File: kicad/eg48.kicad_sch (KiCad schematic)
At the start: 110 parts, among them SW1 PG1350, SW10 PG1350, SW11 PG1350, SW12 PG1350, SW13 PG1350, SW14 PG1350, SW15 PG1350, SW16 PG1350, SW17 PG1350, SW18 PG1350, SW19 PG1350, SW2 PG1350, SW20 PG1350, SW21 PG1350, SW22 PG1350, SW23 PG1350, SW24 PG1350, SW25 PG1350, SW26 PG1350, SW27 PG1350, SW28 PG1350, SW29 PG1350, SW3 PG1350, SW30 PG1350, SW31 PG1350, SW32 PG1350, SW33 PG1350, SW34 PG1350, SW35 PG1350, SW36 PG1350, SW37 PG1350, SW38 PG1350, SW39 PG1350, SW4 PG1350, SW40 PG1350, SW41 PG1350, SW42 PG1350, SW43 PG1350, SW44 PG1350, SW45 PG1350, SW46 PG1350, SW47 PG1350, SW48 PG1350, SW49 RotaryEncoder_Switch_MP, SW5 PG1350, SW6 PG1350, SW7 PG1350, SW8 PG1350, SW9 PG1350

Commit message: Update kicad files, add 3D models
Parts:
- SW49: value RotaryEncoder_Switch_MP -> EC11E12
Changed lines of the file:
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@@
 			)
 		)
-		(property "Value" "RotaryEncoder_Switch_MP"
+		(property "Value" "EC11E12"
 			(at 52.07 77.4699 90)
 			(effects

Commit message: Kicad 9, nicer routing, clearance for rp2040
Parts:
- U1: value ~ -> Pro Micro RP2040; footprint pro_micro_rp2040:pro_micro_rp2040 -> pro_micro_rp2040:pro_micro_rp2040_min; symbol pro_micro_rp2040:pro_micro_rp2040 -> pro_micro_rp2040:pro_micro_rp2040_min
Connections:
- no-connect marks 13 -> 9
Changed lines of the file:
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@@
 (kicad_sch
-	(version 20231120)
+	(version 20250114)
 	(generator "eeschema")
-	(generator_version "8.0")
+	(generator_version "9.0")
 	(paper "A4")
 	(junction
@@
 	)
 	(no_connect
-		(at 50.8 21.59)
-	)
-	(no_connect
 		(at 29.21 54.61)
 	)
 	(no_connect
-		(at 45.72 21.59)
-	)
-	(no_connect
 		(at 40.64 62.23)
 	)
 	(no_connect
-		(at 43.18 21.59)
-	)
-	(no_connect
-		(at 48.26 21.59)
-	)
-	(no_connect
 		(at 60.96 26.67)
 	)
@@
 	(label "ROW9"
 		(at 53.34 64.77 0)
-		(fields_autoplaced yes)
 		(effects
 			(font
@@
 	(label "COL2"
 		(at 63.5 41.91 0)
-		(fields_autoplaced yes)
 		(effects
 			(font
@@
 	(label "COL1"
 		(at 63.5 44.45 0)
-		(fields_autoplaced yes)
 		(effects
 			(font
@@
 	(label "COL5"
 		(at 29.21 29.21 180)
-		(fields_autoplaced yes)
 		(effects
 			(font
@@
 	(label "COL4"
 		(at 80.01 104.14 90)
-		(fields_autoplaced yes)
 		(effects
 			(font
@@
 	(label "COL3"
 		(at 63.5 39.37 0)
-		(fields_autoplaced yes)
 		(effects
 			(font
@@
 	(label "ROW2"
 		(at 142.24 114.3 180)
-		(fields_autoplaced yes)
 		(effects
 			(font
@@
 	(label "COL3"
 		(at 64.77 104.14 90)
-		(fields_autoplaced yes)
 		(effects
 			(font
@@
 	(label "COL6"
 		(at 220.98 104.14 90)
-		(fields_autoplaced yes)
 		(effects
 			(font
@@
 	(label "COL6"
 		(at 110.49 104.14 90)
-		(fields_autoplaced yes)
 		(effects
 			(font
@@
 	(label "ROW7"
 		(at 123.19 160.02 0)
-		(fields_autoplaced yes)
 		(effects
 			(font
@@
 	(label "ROW6"
 		(at 142.24 144.78 180)
-		(fields_autoplaced yes)
 		(effects
 			(font
@@
 	(label "ROW4"
 		(at 63.5 49.53 0)
-		(fields_autoplaced yes)
 		(effects
 			(font
@@
 	(label "COL1"
 		(at 144.78 104.14 90)
-		(fields_autoplaced yes)
 		(effects
 			(font
@@
 	(label "COL5"
 		(at 95.25 104.14 90)
-		(fields_autoplaced yes)
 		(effects
 			(font
@@
 	(label "ROW2"
 		(at 63.5 46.99 0)
-		(fields_autoplaced yes)
 		(effects
 			(font
@@
 	(label "COL4"
 		(at 29.21 26.67 180)
-		(fields_autoplaced yes)
 		(effects
 			(font
@@
 	(label "COL2"
 		(at 160.02 104.14 90)
-		(fields_autoplaced yes)
 		(effects
 			(font
@@
 	(label "ROW8"
 		(at 142.24 160.02 180)
-		(fields_autoplaced yes)
 		(effects
 			(font
@@
 	(label "COL4"
 		(at 190.5 104.14 90)
-		(fields_autoplaced yes)
 		(effects
 			(font
@@
 	(label "COL3"
 		(at 175.26 104.14 90)
-		(fields_autoplaced yes)
 		(effects
 			(font
@@
 	(label "ROW6"
 		(at 63.5 52.07 0)
-		(fields_autoplaced yes)
 		(effects
 			(font
@@
 	(label "LED"
 		(at 88.9 38.1 180)
-		(fields_autoplaced yes)
 		(effects
 			(font
@@
 	(label "COL2"
 		(at 49.53 104.14 90)
-		(fields_autoplaced yes)
 		(effects
 			(font
@@
 	(label "ROW1"
 		(at 29.21 39.37 180)
-		(fields_autoplaced yes)
 		(effects
 			(font
@@
 	(label "ROW5"
 		(at 123.19 144.78 0)
-		(fields_autoplaced yes)
 		(effects
 			(font
@@
 	(label "ROW7"
 		(at 29.21 46.99 180)
-		(fields_autoplaced yes)
 		(effects
 			(font
@@
 	(label "COL5"
 		(at 205.74 104.14 90)
-		(fields_autoplaced yes)
 		(effects
 			(font
@@
 	(label "COL1"
 		(at 34.29 104.14 90)
-		(fields_autoplaced yes)
 		(effects
 			(font
@@
 	(label "LED"
 		(at 29.21 49.53 180)
-		(fields_autoplaced yes)
 		(effects
 			(font
@@
 	(label "ROW8"
 		(at 63.5 54.61 0)
-		(fields_autoplaced yes)
 		(effects
 			(font
@@
 	(label "COL6"
 		(at 29.21 31.75 180)
-		(fields_autoplaced yes)
 		(effects
 			(font
@@
 	(label "ROW4"
 		(at 142.24 129.54 180)
-		(fields_autoplaced yes)
 		(effects
 			(font
@@
 	(label "ROW9"
 		(at 50.8 86.36 0)
-		(fields_autoplaced yes)
 		(effects
 			(font
@@
 	(label "ROW3"
 		(at 123.19 129.54 0)
-		(fields_autoplaced yes)
 		(effects
 			(font
@@
 	(label "ROW5"
 		(at 29.21 44.45 180)
-		(fields_autoplaced yes)
 		(effects
 			(font
@@
 	(label "ROW1"
 		(at 123.19 114.3 0)
-		(fields_autoplaced yes)
 		(effects
 			(font
@@
 	(label "COL6"
 		(at 50.8 88.9 0)
-		(fields_autoplaced yes)
 		(effects
 			(font
@@
 	(label "ROW3"
 		(at 29.21 41.91 180)
-		(fields_autoplaced yes)
 		(effects
 			(font
@@
 	)
 	(symbol
-		(lib_id "pro_micro_rp2040:pro_micro_rp2040")
+		(lib_id "pro_micro_rp2040:pro_micro_rp2040_min")
 		(at 45.72 41.91 0)
 		(unit 1)
@@
 		(fields_autoplaced yes)
 		(property "Reference" "U1"
-			(at 52.9941 20.32 0)
+			(at 46.355 20.32 0)
 			(effects
 				(font
 					(size 1.27 1.27)
 				)
-				(justify left)
 			)
 		)
-		(property "Value" "~"
-			(at 52.9941 22.86 0)
+		(property "Value" "Pro Micro RP2040"
+			(at 46.355 22.86 0)
 			(effects
 				(font
 					(size 1.27 1.27)
 				)
-				(justify left)
 			)
 		)
-		(property "Footprint" "pro_micro_rp2040:pro_micro_rp2040"
+		(property "Footprint" "pro_micro_rp2040:pro_micro_rp2040_min"
 			(at 57.15 20.32 0)
 			(effects
@@
 		(pin "8"
 		)
-		(pin "BOOT"
-		)
 		(pin "5"
 		)
@@
 		(pin "20"
 		)
-		(pin "24"
-		)
-		(pin "18"
-		)
 		(pin "29"
 		)
@@
 		(pin "16"
 		)
-		(pin "25"
-		)
 		(pin "6"
 		)
@@
 		)
 	)
+	(embedded_fonts no)
 )

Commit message: Make diodes more obvious, make text nicer
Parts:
- D1, D10, D11, D12, D13, D14, D15, D16, D17, D18, D19, D2, D20, D21, D22, D23, D24, D25, D26, D27, D28, D29, D3, D30, D31, D32, D33, D34, D35, D36, D37, D38, D39, D4, D40, D41, D42, D43, D44, D45, D46, D47, D48, D5, D6, D7, D8, D9: footprint Diode_SMD:D_SOD-123 -> diodes:D_SOD-123
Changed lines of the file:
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@@
 			)
 		)
-		(property "Footprint" "Diode_SMD:D_SOD-123"
+		(property "Footprint" "diodes:D_SOD-123"
 			(at 55.245 125.73 0)
 			(effects
@@
 			)
 		)
-		(property "Footprint" "Diode_SMD:D_SOD-123"
+		(property "Footprint" "diodes:D_SOD-123"
 			(at 85.725 125.73 0)
 			(effects
@@
 			)
 		)
-		(property "Footprint" "Diode_SMD:D_SOD-123"
+		(property "Footprint" "diodes:D_SOD-123"
 			(at 116.205 140.97 0)
 			(effects
@@
 			)
 		)
-		(property "Footprint" "Diode_SMD:D_SOD-123"
+		(property "Footprint" "diodes:D_SOD-123"
 			(at 116.205 110.49 0)
 			(effects
@@
 			)
 		)
-		(property "Footprint" "Diode_SMD:D_SOD-123"
+		(property "Footprint" "diodes:D_SOD-123"
 			(at 40.005 125.73 0)
 			(effects
@@
 			)
 		)
-		(property "Footprint" "Diode_SMD:D_SOD-123"
+		(property "Footprint" "diodes:D_SOD-123"
 			(at 196.215 140.97 0)
 			(effects
@@
 			)
 		)
-		(property "Footprint" "Diode_SMD:D_SOD-123"
+		(property "Footprint" "diodes:D_SOD-123"
 			(at 180.975 110.49 0)
 			(effects
@@
 			)
 		)
-		(property "Footprint" "Diode_SMD:D_SOD-123"
+		(property "Footprint" "diodes:D_SOD-123"
 			(at 85.725 110.49 0)
 			(effects
@@
 			)
 		)
-		(property "Footprint" "Diode_SMD:D_SOD-123"
+		(property "Footprint" "diodes:D_SOD-123"
 			(at 211.455 140.97 0)
 			(effects
@@
 			)
 		)
-		(property "Footprint" "Diode_SMD:D_SOD-123"
+		(property "Footprint" "diodes:D_SOD-123"
 			(at 196.215 125.73 0)
 			(effects
@@
 			)
 		)
-		(property "Footprint" "Diode_SMD:D_SOD-123"
+		(property "Footprint" "diodes:D_SOD-123"
 			(at 211.455 156.21 0)
 			(effects
@@
 			)
 		)
-		(property "Footprint" "Diode_SMD:D_SOD-123"
+		(property "Footprint" "diodes:D_SOD-123"
 			(at 85.725 140.97 0)
 			(effects
@@
 			)
 		)
-		(property "Footprint" "Diode_SMD:D_SOD-123"
+		(property "Footprint" "diodes:D_SOD-123"
 			(at 226.695 140.97 0)
 			(effects
@@
 			)
 		)
-		(property "Footprint" "Diode_SMD:D_SOD-123"
+		(property "Footprint" "diodes:D_SOD-123"
 			(at 196.215 110.49 0)
 			(effects
@@
 			)
 		)
-		(property "Footprint" "Diode_SMD:D_SOD-123"
+		(property "Footprint" "diodes:D_SOD-123"
 			(at 180.975 125.73 0)
 			(effects
@@
 			)
 		)
-		(property "Footprint" "Diode_SMD:D_SOD-123"
+		(property "Footprint" "diodes:D_SOD-123"
 			(at 165.735 110.49 0)
 			(effects
@@
 			)
 		)
-		(property "Footprint" "Diode_SMD:D_SOD-123"
+		(property "Footprint" "diodes:D_SOD-123"
 			(at 165.735 140.97 0)
 			(effects
@@
 			)
 		)
-		(property "Footprint" "Diode_SMD:D_SOD-123"
+		(property "Footprint" "diodes:D_SOD-123"
 			(at 100.965 125.73 0)
 			(effects
@@
 			)
 		)
-		(property "Footprint" "Diode_SMD:D_SOD-123"
+		(property "Footprint" "diodes:D_SOD-123"
 			(at 180.975 156.21 0)
 			(effects
@@
 			)
 		)
-		(property "Footprint" "Diode_SMD:D_SOD-123"
+		(property "Footprint" "diodes:D_SOD-123"
 			(at 40.005 110.49 0)
 			(effects
@@
 			)
 		)
-		(property "Footprint" "Diode_SMD:D_SOD-123"
+		(property "Footprint" "diodes:D_SOD-123"
 			(at 196.215 156.21 0)
 			(effects
@@
 			)
 		)
-		(property "Footprint" "Diode_SMD:D_SOD-123"
+		(property "Footprint" "diodes:D_SOD-123"
 			(at 40.005 156.21 0)
 			(effects
@@
 			)
 		)
-		(property "Footprint" "Diode_SMD:D_SOD-123"
+		(property "Footprint" "diodes:D_SOD-123"
 			(at 55.245 110.49 0)
 			(effects
@@
 			)
 		)
-		(property "Footprint" "Diode_SMD:D_SOD-123"
+		(property "Footprint" "diodes:D_SOD-123"
 			(at 150.495 110.49 0)
 			(effects
@@
 			)
 		)
-		(property "Footprint" "Diode_SMD:D_SOD-123"
+		(property "Footprint" "diodes:D_SOD-123"
 			(at 226.695 125.73 0)
 			(effects
@@
 			)
 		)
-		(property "Footprint" "Diode_SMD:D_SOD-123"
+		(property "Footprint" "diodes:D_SOD-123"
 			(at 85.725 156.21 0)
 			(effects
@@
 			)
 		)
-		(property "Footprint" "Diode_SMD:D_SOD-123"
+		(property "Footprint" "diodes:D_SOD-123"
 			(at 116.205 156.21 0)
 			(effects
@@
 			)
 		)
-		(property "Footprint" "Diode_SMD:D_SOD-123"
+		(property "Footprint" "diodes:D_SOD-123"
 			(at 70.485 156.21 0)
 			(effects
@@
 			)
 		)
-		(property "Footprint" "Diode_SMD:D_SOD-123"
+		(property "Footprint" "diodes:D_SOD-123"
 			(at 211.455 125.73 0)
 			(effects
@@
 			)
 		)
-		(property "Footprint" "Diode_SMD:D_SOD-123"
+		(property "Footprint" "diodes:D_SOD-123"
 			(at 180.975 140.97 0)
 			(effects
@@
 			)
 		)
-		(property "Footprint" "Diode_SMD:D_SOD-123"
+		(property "Footprint" "diodes:D_SOD-123"
 			(at 100.965 110.49 0)
 			(effects
@@
 			)
 		)
-		(property "Footprint" "Diode_SMD:D_SOD-123"
+		(property "Footprint" "diodes:D_SOD-123"
 			(at 150.495 140.97 0)
 			(effects
@@
 			)
 		)
-		(property "Footprint" "Diode_SMD:D_SOD-123"
+		(property "Footprint" "diodes:D_SOD-123"
 			(at 150.495 156.21 0)
 			(effects
@@
 			)
 		)
-		(property "Footprint" "Diode_SMD:D_SOD-123"
+		(property "Footprint" "diodes:D_SOD-123"
 			(at 100.965 156.21 0)
 			(effects
@@
 			)
 		)
-		(property "Footprint" "Diode_SMD:D_SOD-123"
+		(property "Footprint" "diodes:D_SOD-123"
 			(at 211.455 110.49 0)
 			(effects
@@
 			)
 		)
-		(property "Footprint" "Diode_SMD:D_SOD-123"
+		(property "Footprint" "diodes:D_SOD-123"
 			(at 226.695 156.21 0)
 			(effects
@@
 			)
 		)
-		(property "Footprint" "Diode_SMD:D_SOD-123"
+		(property "Footprint" "diodes:D_SOD-123"
 			(at 165.735 156.21 0)
 			(effects
@@
 			)
 		)
-		(property "Footprint" "Diode_SMD:D_SOD-123"
+		(property "Footprint" "diodes:D_SOD-123"
 			(at 70.485 140.97 0)
 			(effects
@@
 			)
 		)
-		(property "Footprint" "Diode_SMD:D_SOD-123"
+		(property "Footprint" "diodes:D_SOD-123"
 			(at 226.695 110.49 0)
 			(effects
@@
 			)
 		)
-		(property "Footprint" "Diode_SMD:D_SOD-123"
+		(property "Footprint" "diodes:D_SOD-123"
 			(at 70.485 125.73 0)
 			(effects
@@
 			)
 		)
-		(property "Footprint" "Diode_SMD:D_SOD-123"
+		(property "Footprint" "diodes:D_SOD-123"
 			(at 100.965 140.97 0)
 			(effects
@@
 			)
 		)
-		(property "Footprint" "Diode_SMD:D_SOD-123"
+		(property "Footprint" "diodes:D_SOD-123"
 			(at 55.245 140.97 0)
 			(effects
@@
 			)
 		)
-		(property "Footprint" "Diode_SMD:D_SOD-123"
+		(property "Footprint" "diodes:D_SOD-123"
 			(at 116.205 125.73 0)
 			(effects
@@
 			)
 		)
-		(property "Footprint" "Diode_SMD:D_SOD-123"
+		(property "Footprint" "diodes:D_SOD-123"
 			(at 55.245 156.21 0)
 			(effects
@@
 			)
 		)
-		(property "Footprint" "Diode_SMD:D_SOD-123"
+		(property "Footprint" "diodes:D_SOD-123"
 			(at 150.495 125.73 0)
 			(effects
@@
 			)
 		)
-		(property "Footprint" "Diode_SMD:D_SOD-123"
+		(property "Footprint" "diodes:D_SOD-123"
 			(at 40.005 140.97 0)
 			(effects
@@
 			)
 		)
-		(property "Footprint" "Diode_SMD:D_SOD-123"
+		(property "Footprint" "diodes:D_SOD-123"
 			(at 165.735 125.73 0)
 			(effects
@@
 			)
 		)
-		(property "Footprint" "Diode_SMD:D_SOD-123"
+		(property "Footprint" "diodes:D_SOD-123"
 			(at 70.485 110.49 0)
 			(effects

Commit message: Unrounded
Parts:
- SW49: footprint Rotary_Encoder:RotaryEncoder_Alps_EC11E-Switch_Vertical_H20mm -> encoders:ec11e12
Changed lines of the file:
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@@
 			)
 		)
-		(property "Footprint" "Rotary_Encoder:RotaryEncoder_Alps_EC11E-Switch_Vertical_H20mm"
+		(property "Footprint" "encoders:ec11e12"
 			(at 49.784 72.39 0)
 			(effects

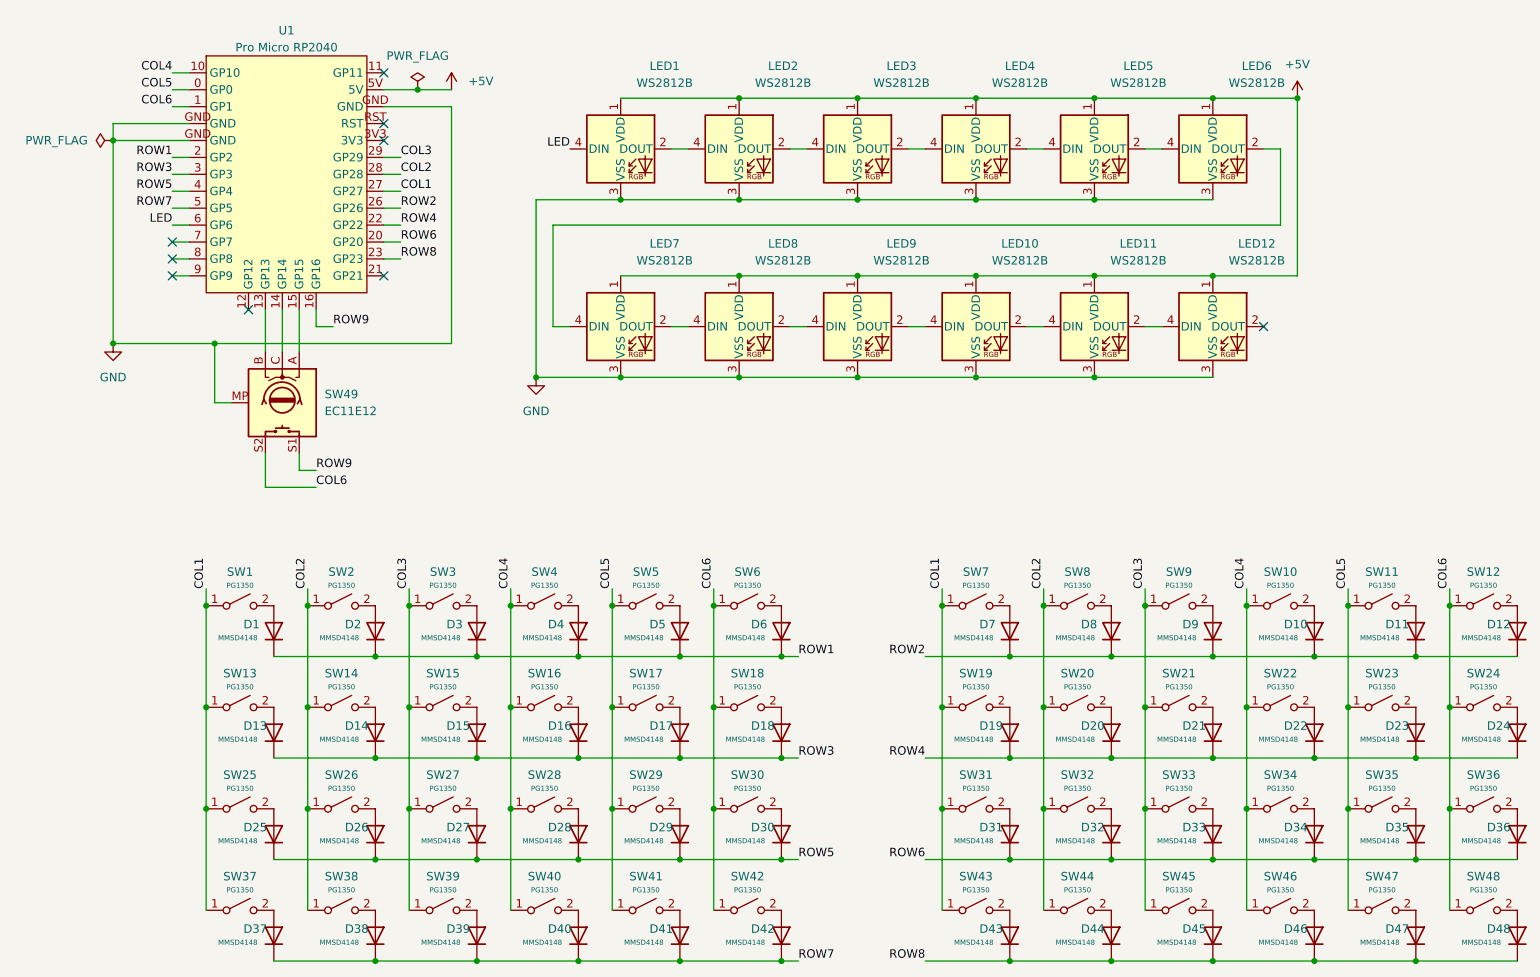
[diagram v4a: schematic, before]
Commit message: Reroute to avoid using bottom pins
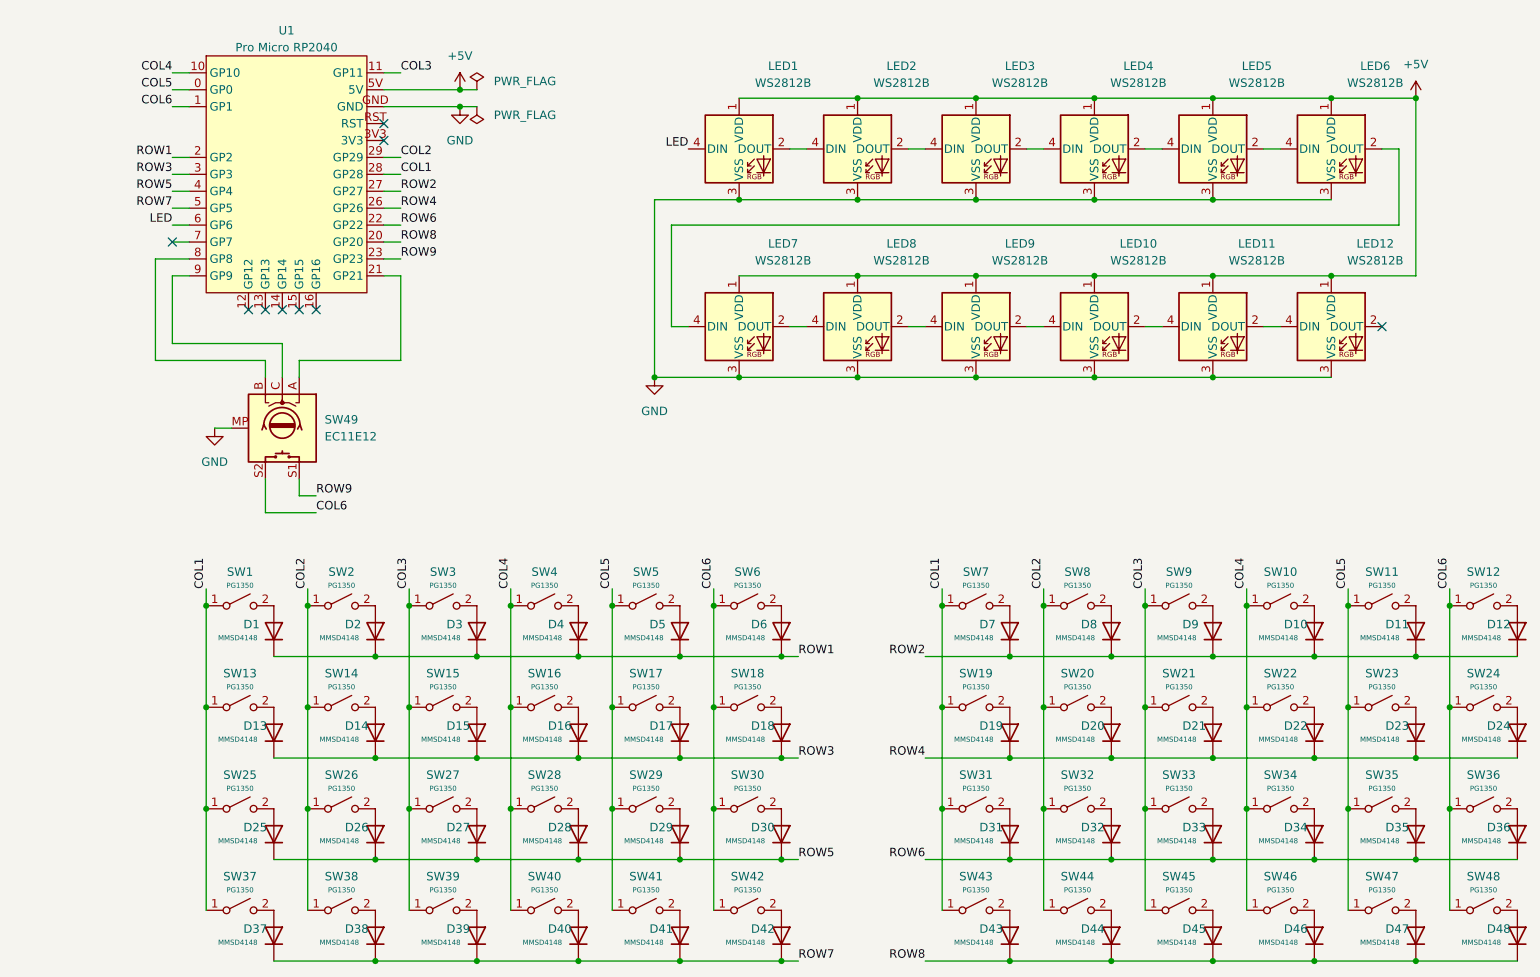
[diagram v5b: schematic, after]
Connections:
- net COL1: now also U1.28 (GP28); no longer U1.27 (GP27)
- net COL2: now also U1.29 (GP29); no longer U1.28 (GP28)
- net COL3: now also U1.11 (GP11); no longer U1.29 (GP29)
- net ROW2: now also U1.27 (GP27); no longer U1.26 (GP26)
- net ROW4: now also U1.26 (GP26); no longer U1.22 (GP22)
- net ROW6: now also U1.22 (GP22); no longer U1.20 (GP20)
- net ROW8: now also U1.20 (GP20); no longer U1.23 (GP23)
- net ROW9: now also U1.23 (GP23); no longer U1.16 (GP16)
- net at U1.13 (GP13): no longer SW49.B
- net at U1.14 (GP14): no longer SW49.C
- net at U1.15 (GP15): no longer SW49.A
- net at U1.21 (GP21): now also SW49.A
- net at U1.8 (GP8): now also SW49.B
- net at U1.9 (GP9): now also SW49.C
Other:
- moved on the sheet: LED1, LED10, LED11, LED12, LED2, LED3, LED4, LED5, LED6, LED7, LED8, LED9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

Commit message: Remove 5 bottom pins
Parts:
- U1: footprint pro_micro_rp2040:pro_micro_rp2040_min -> pro_micro_rp2040:pro_micro_rp2040_min_nobot; symbol pro_micro_rp2040:pro_micro_rp2040_min -> pro_micro_rp2040:pro_micro_rp2040_min_nobot
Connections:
- no-connect marks 9 -> 4
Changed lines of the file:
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@@
-	)
-	(no_connect
-		(at 40.64 62.23)
 	)
 	(no_connect
@@
 	)
 	(no_connect
-		(at 43.18 62.23)
-	)
-	(no_connect
-		(at 48.26 62.23)
-	)
-	(no_connect
-		(at 50.8 62.23)
-	)
-	(no_connect
 		(at 29.21 52.07)
 	)
@@
 	)
 	(no_connect
-		(at 45.72 62.23)
-	)
-	(no_connect
 		(at 210.82 64.77)
 	)
@@
 	)
 	(symbol
-		(lib_id "pro_micro_rp2040:pro_micro_rp2040_min")
+		(lib_id "pro_micro_rp2040:pro_micro_rp2040_min_nobot")
 		(at 45.72 41.91 0)
 		(unit 1)
@@
 		(fields_autoplaced yes)
 		(property "Reference" "U1"
-			(at 46.355 20.32 0)
+			(at 46.355 19.05 0)
 			(effects
 				(font
@@
 		)
 		(property "Value" "Pro Micro RP2040"
-			(at 46.355 22.86 0)
+			(at 46.355 21.59 0)
 			(effects
 				(font
@@
 			)
 		)
-		(property "Footprint" "pro_micro_rp2040:pro_micro_rp2040_min"
+		(property "Footprint" "pro_micro_rp2040:pro_micro_rp2040_min_nobot"
 			(at 57.15 20.32 0)
 			(effects
@@
 		(pin "26"
 		)
-		(pin "14"
-		)
 		(pin "1"
 		)
-		(pin "13"
-		)
 		(pin "GND"
 		)
@@
 		(pin "9"
 		)
-		(pin "15"
-		)
 		(pin "7"
 		)
@@
 		(pin "11"
 		)
-		(pin "12"
-		)
 		(pin "28"
 		)
-		(pin "16"
-		)
 		(pin "6"
